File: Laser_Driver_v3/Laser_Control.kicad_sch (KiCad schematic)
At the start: 10 parts, among them U30 74AHCT125, U31 AD9833xRM, U32 AD5064BRUZ, U33 AD9833xRM

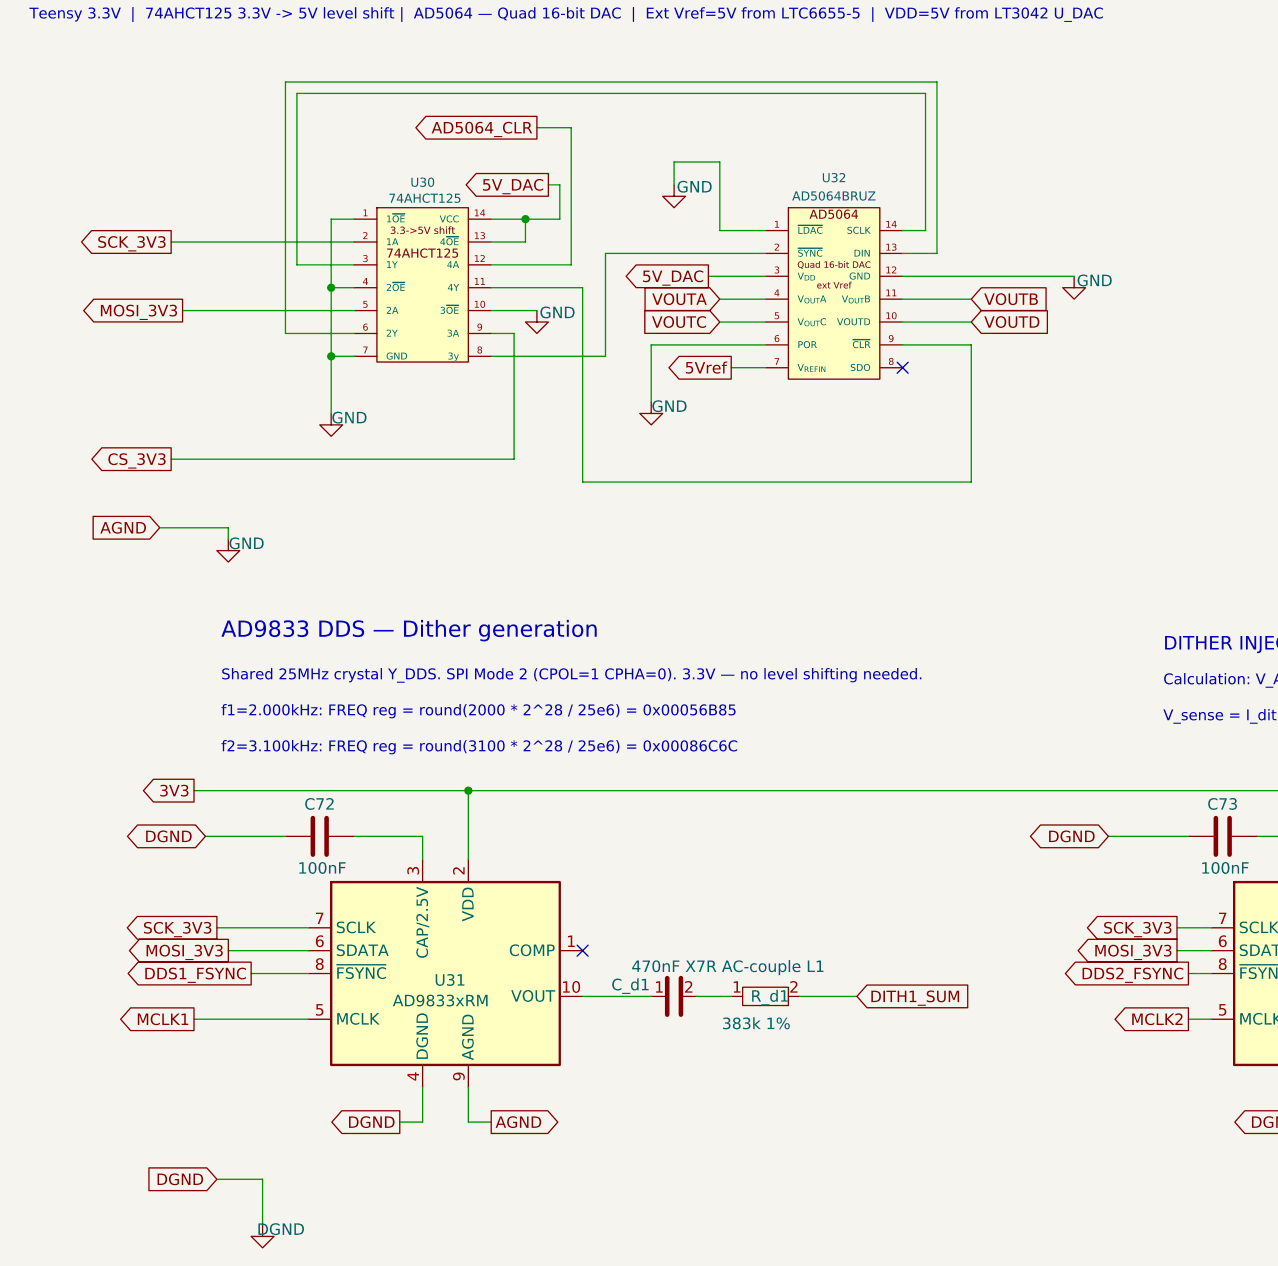
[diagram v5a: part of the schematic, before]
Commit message: Many changes.  Working through ERC.
Main changes are for the grounds.  I found the NETTIE function to tie the GND, DGND and AGND together at a specific point on the boud with a footprint even.
Changed transformers one more time to be consistent for both.
Updated footprints to be consistent and avoid power input/output errors with the ERC.
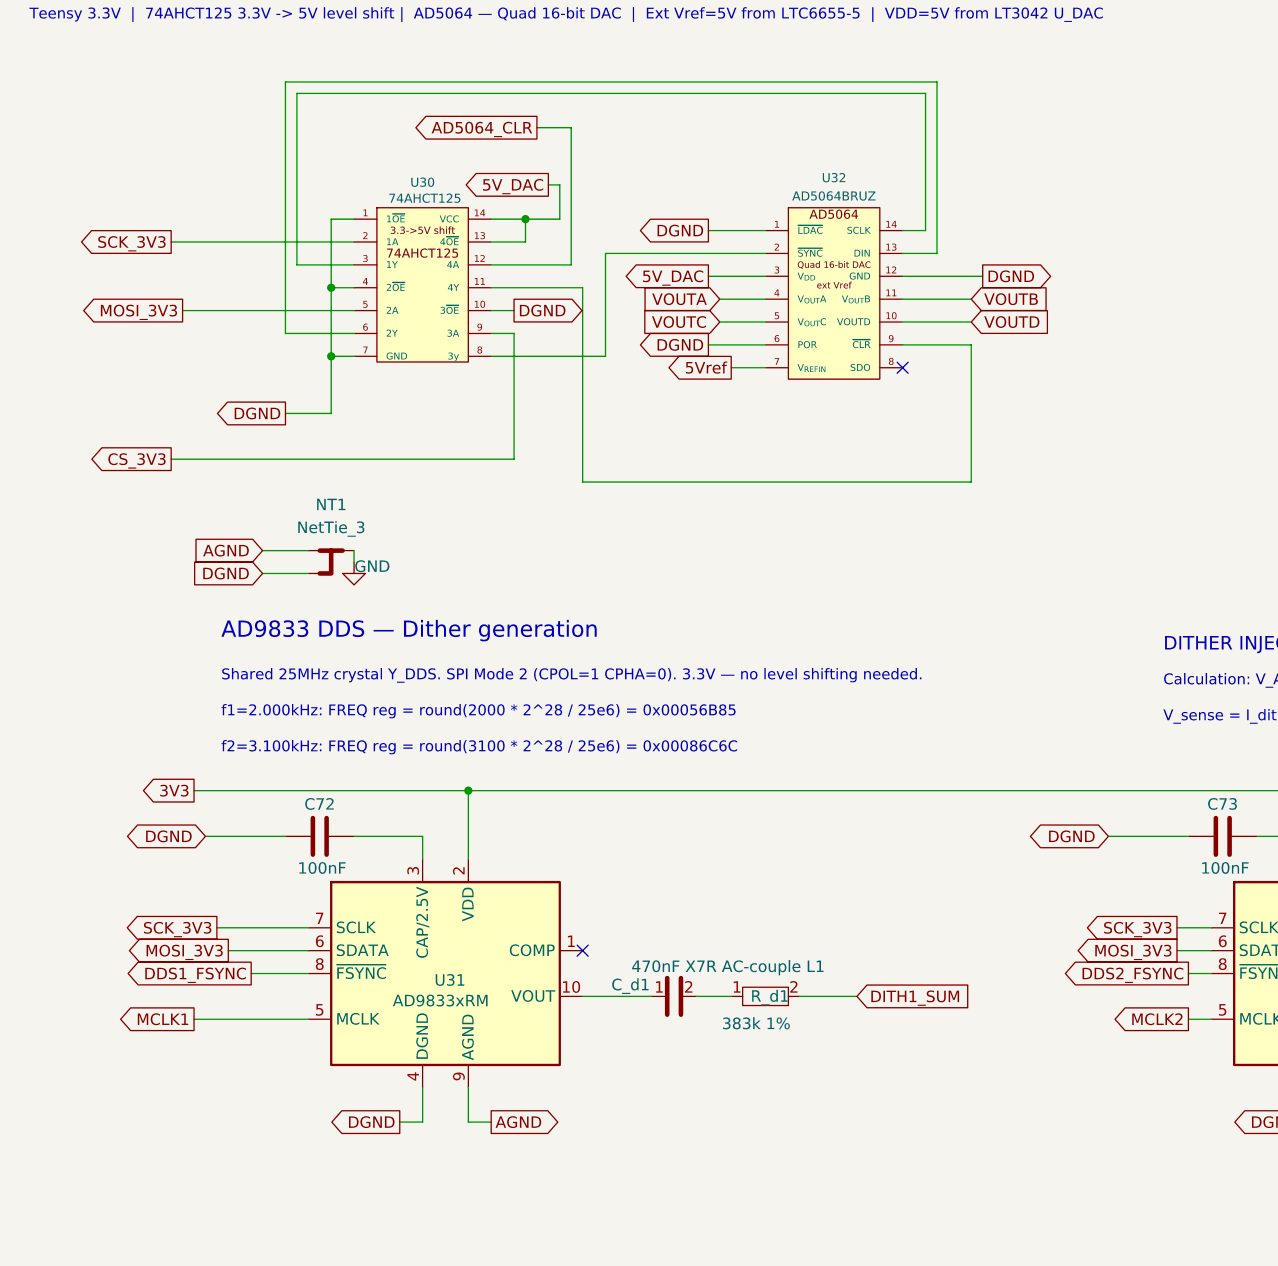
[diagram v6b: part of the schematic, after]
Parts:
- added NT1: NetTie_3, NetTie:NetTie-3_THT_Pad1.0mm, symbol Device:NetTie_3
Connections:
- net DGND: now also U30.1 (1~{OE}), U30.10 (3~{OE}), U30.4 (2~{OE}), U30.7 (GND), U32.1 (~{LDAC}), U32.12 (GND), U32.6 (POR), NT1.3
- net GND: now also NT1.2; no longer U30.1 (1~{OE}), U30.10 (3~{OE}), U30.4 (2~{OE}), U30.7 (GND), U31.9 (AGND), U32.1 (~{LDAC}), U32.12 (GND), U32.6 (POR), U33.9 (AGND)
- new net AGND: NT1.1, U31.9 (AGND), U33.9 (AGND)

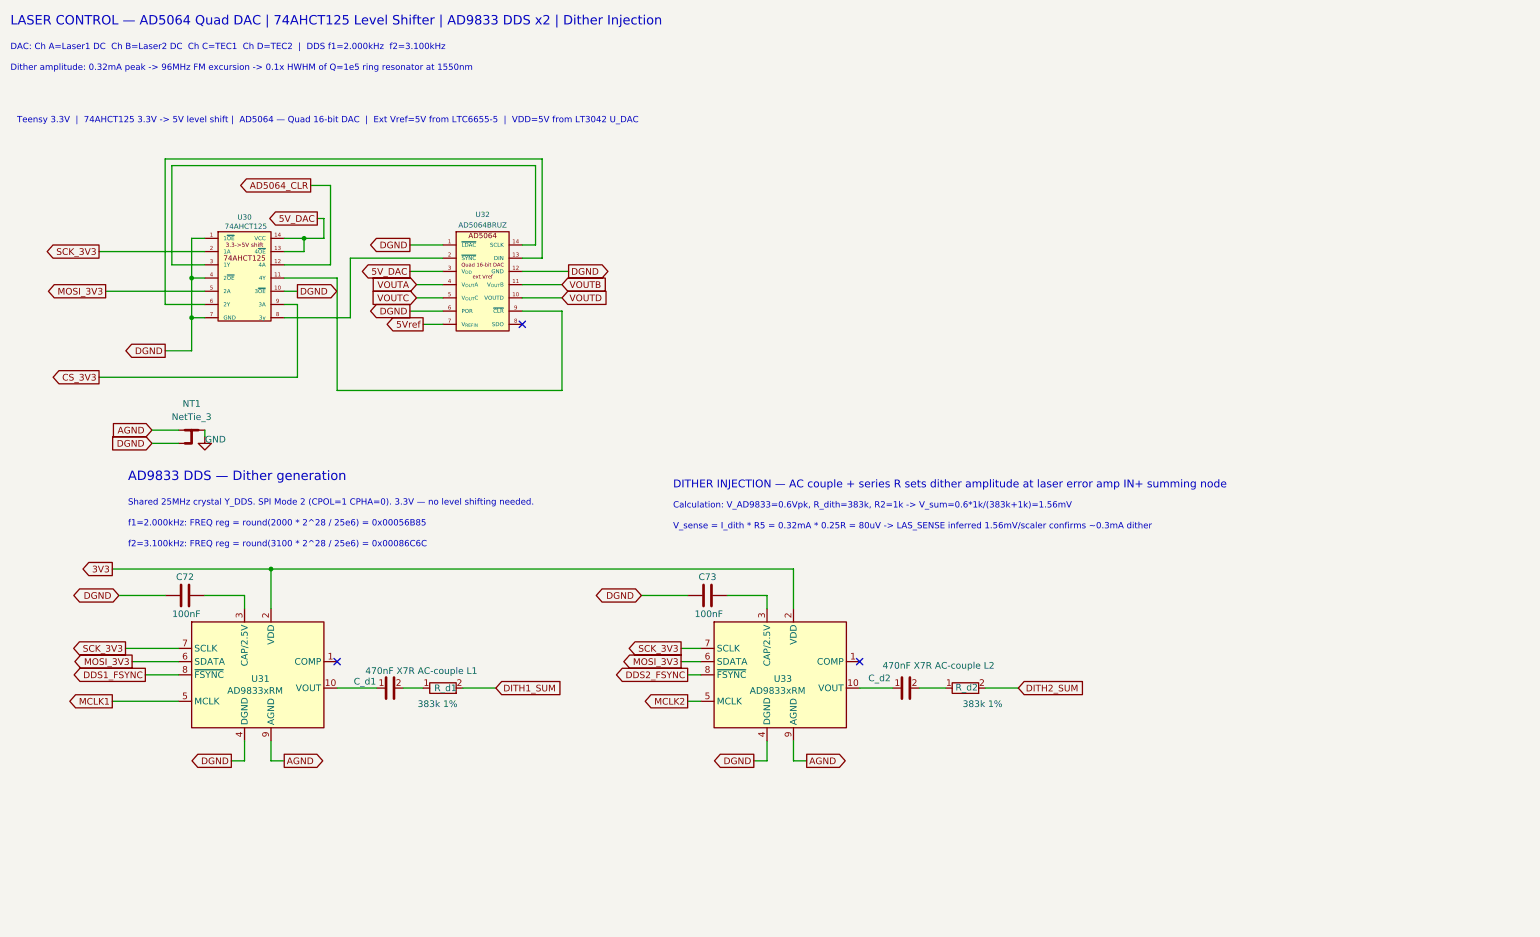
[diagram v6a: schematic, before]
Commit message: Changed to an RF modulation
Based on the uncertainty calculation, needed to change from a low frequency modulation to an RF modulation.  This drive down the noise, but required a very different implentation.  The modulation is limited to about 2 MHz.  Much faster is at the limit of this hardware and would require significant increase in complexity and cost.
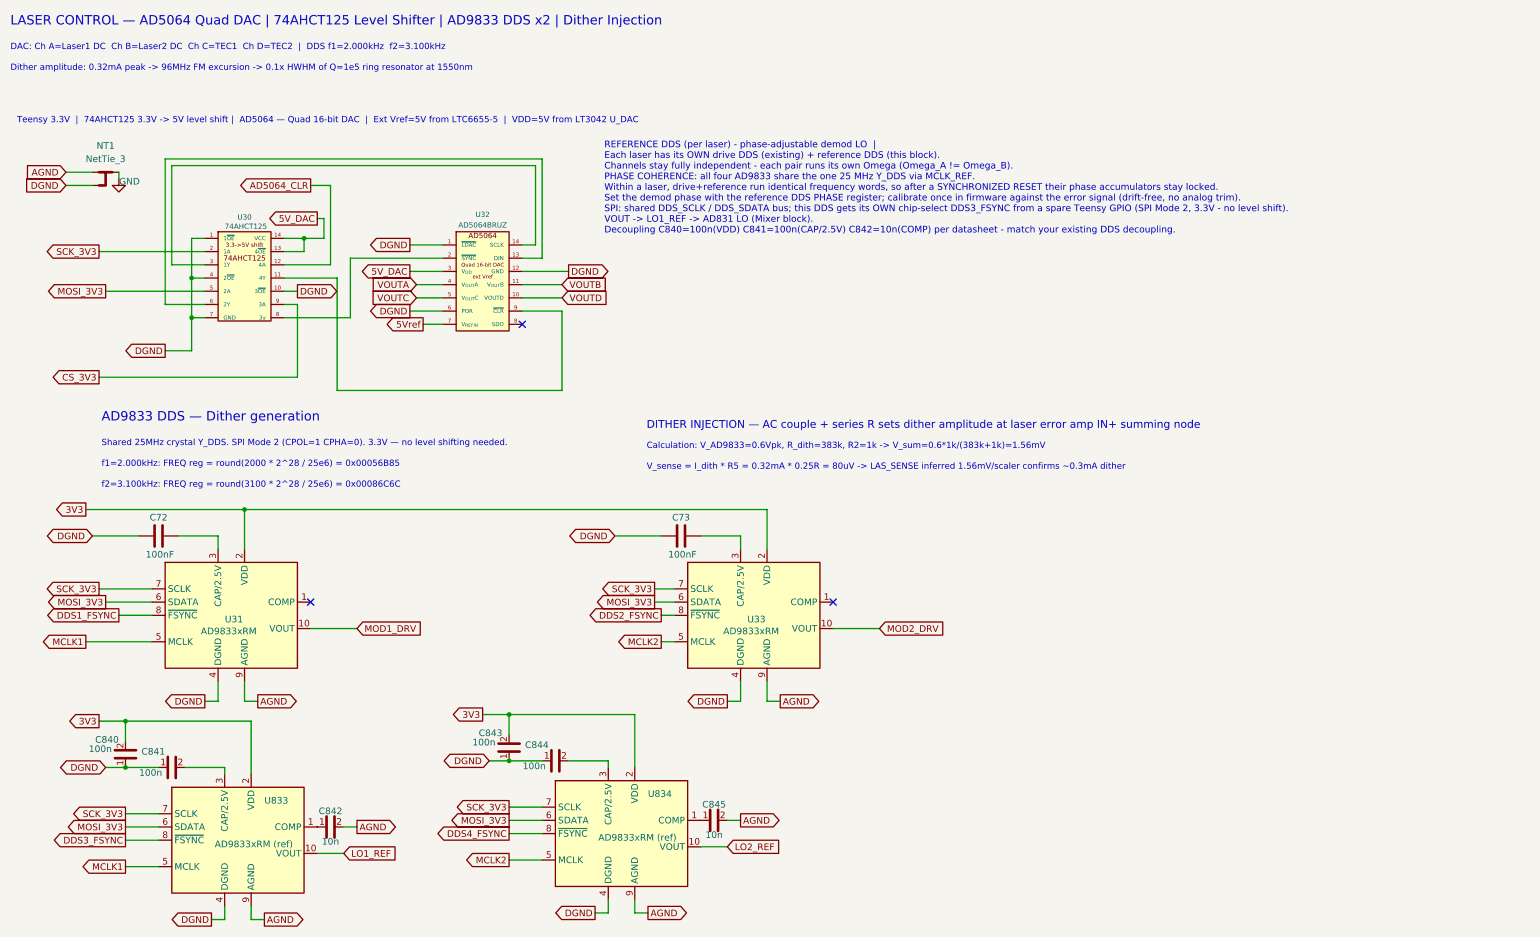
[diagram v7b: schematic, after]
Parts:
- removed C_d1: 470nF X7R AC-couple L1, Capacitor_SMD:C_0805_2012Metric_Pad1.18x1.45mm_HandSolder, symbol Device:C
- removed C_d2: 470nF X7R AC-couple L2, Capacitor_SMD:C_0805_2012Metric_Pad1.18x1.45mm_HandSolder, symbol Device:C
- removed R_d1, R_d2: 383k 1%, Resistor_SMD:R_0805_2012Metric_Pad1.20x1.40mm_HandSolder, symbol Device:R
- added C840, C841, C843, C844: 100n, symbol Device:C
- added C842, C845: 10n, symbol Device:C
- added U833, U834: AD9833xRM (ref), symbol Interface:AD9833xRM
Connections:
- net 3V3: now also C840.2, C843.2, U833.2 (VDD), U834.2 (VDD)
- net AGND: now also C842.2, C845.2, U833.9 (AGND), U834.9 (AGND)
- net DGND: now also C840.1, C841.1, C843.1, C844.1, U833.4 (DGND), U834.4 (DGND)
- net MCLK1: now also U833.5 (MCLK)
- net MCLK2: now also U834.5 (MCLK)
- net MOSI_3V3: now also U833.6 (SDATA), U834.6 (SDATA)
- net SCK_3V3: now also U833.7 (SCLK), U834.7 (SCLK)
- net MOD1_DRV: now reaches U31.10 (VOUT)
- net MOD2_DRV: now reaches U33.10 (VOUT)
- new net: C841.2, U833.3 (CAP/2.5V)
- new net: C842.1, U833.1 (COMP)
- new net: C845.1, U834.1 (COMP)
- new net: C844.2, U834.3 (CAP/2.5V)
- new net DDS3_FSYNC: U833.8 (~{FSYNC})
- new net DDS4_FSYNC: U834.8 (~{FSYNC})
- new net LO1_REF: U833.10 (VOUT)
- new net LO2_REF: U834.10 (VOUT)
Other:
- note added: "REFERENCE DDS (per laser) - phase-adjustable demod LO | Each laser has its OWN drive DDS (existing) + reference DDS (this block). Channels stay fully independent - each pair runs its own Omega (Omega_A != Omega_B). PHASE COHERENCE: all four AD9833 share the one 25 MHz Y_DDS via MCLK_REF. Within a laser, drive+reference run identical frequency words, so after a SYNCHRONIZED RESET their phase accum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"
- moved on the sheet: C72, C73, NT1, U31, U33
